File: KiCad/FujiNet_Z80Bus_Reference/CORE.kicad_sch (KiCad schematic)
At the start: 23 parts, among them IC1 74244N, IC13 7432N, IC2 7404N, IC3 7474N, IC5 7408N

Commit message: Single PCB layout experiements
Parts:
- renumbered IC1 to ESP_CONTROL_DIRECTOR1, RN1 to ESP_CONTROL_DIRECTOR_BIAS1
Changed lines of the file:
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@@
   (symbol (lib_id "FujiNet_Z80Bus_Reference-rescue:4609M-101-103LF-Z80ESP-eagle-import") (at 140.97 167.64 0) (mirror y) (unit 1)
     (in_bom yes) (on_board yes) (dnp no)
-    (property "Reference" "RN1" (at 128.27 171.45 90)
-      (effects (font (size 1.4986 1.4986)) (justify left))
+    (property "Reference" "ESP_CONTROL_DIRECTOR_BIAS1" (at 128.27 171.45 90)
+      (effects (font (size 1.4986 1.4986)))
     )
     (property "Value" "4609M-101-103LF" (at 130.81 189.23 90)
@@
       (project "FujiNet_Z80Bus_Reference"
         (path "/532c0392-800e-45cc-8170-6d32f2390e83/00000000-0000-0000-0000-000068f578e9"
-          (reference "RN1") (unit 1)
+          (reference "ESP_CONTROL_DIRECTOR_BIAS1") (unit 1)
         )
         (path "/532c0392-800e-45cc-8170-6d32f2390e83/00000000-0000-0000-0000-000068f578e9/00000000-0000-0000-0000-000068fd7452"
@@
   (symbol (lib_id "FujiNet_Z80Bus_Reference-rescue:74244N-Z80ESP-eagle-import") (at 88.9 153.67 0) (unit 1)
     (in_bom yes) (on_board yes) (dnp no)
-    (property "Reference" "IC1" (at 90.17 157.48 90)
-      (effects (font (size 1.4986 1.4986)) (justify left bottom))
+    (property "Reference" "ESP_CONTROL_DIRECTOR1" (at 90.17 157.48 90)
+      (effects (font (size 1.4986 1.4986)))
     )
     (property "Value" "74244N" (at 81.28 166.37 0)
@@
       (project "FujiNet_Z80Bus_Reference"
         (path "/532c0392-800e-45cc-8170-6d32f2390e83/00000000-0000-0000-0000-000068f578e9"
-          (reference "IC1") (unit 1)
+          (reference "ESP_CONTROL_DIRECTOR1") (unit 1)
         )
         (path "/532c0392-800e-45cc-8170-6d32f2390e83/00000000-0000-0000-0000-000068f578e9/00000000-0000-0000-0000-000068fd7452"
@@
   (symbol (lib_id "FujiNet_Z80Bus_Reference-rescue:74244N-Z80ESP-eagle-import") (at 88.9 172.72 0) (unit 2)
     (in_bom yes) (on_board yes) (dnp no)
-    (property "Reference" "IC1" (at 90.17 176.53 90)
-      (effects (font (size 1.4986 1.4986)) (justify left bottom))
+    (property "Reference" "ESP_CONTROL_DIRECTOR1" (at 90.17 176.53 90)
+      (effects (font (size 1.4986 1.4986)))
     )
     (property "Value" "74244N" (at 81.28 185.42 0)
@@
       (project "FujiNet_Z80Bus_Reference"
         (path "/532c0392-800e-45cc-8170-6d32f2390e83/00000000-0000-0000-0000-000068f578e9"
-          (reference "IC1") (unit 2)
-        )
-        (path "/532c0392-800e-45cc-8170-6d32f2390e83/00000000-0000-0000-0000-000068f578e9/00000000-0000-0000-0000-000068fd7452"
+          (reference "ESP_CONTROL_DIRECTOR1") (unit 2)
+        )
+        (path "/532c0392-800e-45cc-8170-6d32f2390e83/00000000-0000-0000-0000-000068f578e9/00000000-0000-0000-0000-000068fd7452"

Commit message: Massive fix to KiCad Labels
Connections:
- net ESP_INT: now also R?.1; no longer R?.2
- net GND: now also R?.2; no longer R?.1
- net VCC: no longer D5.2 (A), R?.1, U?.19 (+5v), U?.20 (+5V)
- net ESP_CONTROL_IORQ renamed ESP_CONTROL.IORQ
- net ESP_CONTROL_MEMRQ renamed ESP_CONTROL.MEMRQ
- net ESP_CONTROL_RD renamed ESP_CONTROL.RD
- net ESP_CONTROL_WR renamed ESP_CONTROL.WR
- net ESP_SPI.CE renamed ESP_SPI_INT.CE
- net ESP_SPI.MISO renamed ESP_SPI_INT.MISO
- net ESP_SPI.MOSI renamed ESP_SPI_INT.MOSI
- net ESP_SPI.OE renamed ESP_SPI_INT.OE
- net ESP_SPI.PL renamed ESP_SPI_INT.PL
- net ESP_SPI.SCK renamed ESP_SPI_INT.SCK
- net ESP_SPI.STC renamed ESP_SPI_INT.STC
- net LOCAL_IORQ renamed LOCAL_CONTROL.IORQ
- net LOCAL_CONTROL.IORQ: now also ESP_CONTROL_DIRECTOR_BIAS1.4; no longer ESP_CONTROL_DIRECTOR_BIAS1.5
- net LOCAL_MEMRQ renamed LOCAL_CONTROL.MEMRQ
- net LOCAL_CONTROL.MEMRQ: now also ESP_CONTROL_DIRECTOR_BIAS1.5; no longer ESP_CONTROL_DIRECTOR_BIAS1.4
- net LOCAL_RD renamed LOCAL_CONTROL.RD
- net LOCAL_WR renamed LOCAL_CONTROL.WR
- net ROM_WR_PROTECT renamed ESP_ROM_WR_PROTECT
- net Z80_BUSACK renamed Z80_CONTROL.BUSACK
- net Z80_IORQ renamed Z80_CONTROL.IORQ
- net Z80_MEMRQ renamed Z80_CONTROL.MEMRQ
- net Z80_RD renamed Z80_CONTROL.RD
- net Z80_RESET renamed Z80_CONTROL.RESET
- net Z80_WAIT renamed Z80_CONTROL.WAIT
- net Z80_WR renamed Z80_CONTROL.WR
- new net +5V: D5.2 (A), R?.1, U?.19 (+5v), U?.20 (+5V)
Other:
- sheet SPIBUS ports: added LOCAL_A[0..15], LOCAL_D[0..7], {ESP_CONTROL}, {ESP_SPI_INTERNAL}, {Z80_CONTROL}; removed ESP_CONTROL_BUSRQ, ESP_CONTROL_IORQ, ESP_CONTROL_MEMRQ, ESP_CONTROL_NMI, ESP_CONTROL_RD, ESP_CONTROL_ROMCS, ESP_CONTROL_WAIT, ESP_CONTROL_WR, ESP_PULSE, ESP_SPI.CE, ESP_SPI.MISO, ESP_SPI.MOSI, ESP_SPI.OE, ESP_SPI.PL, ESP_SPI.SCK, ESP_SPI.STC, LOCAL_ADD_[0..15], LOCAL_DATA_[0..7], Z80_BUSACK, Z80_BUSRQ, Z80_IORQ, Z80_MEMRQ, Z80_NMI, Z80_RD, Z80_ROMCS, Z80_WAIT, Z80_WR
- moved on the sheet: C1, C2, D13, D2, D3, D5, D?, ESP_CONTROL_DIRECTOR1A, ESP_CONTROL_DIRECTOR1B, ESP_CONTROL_DIRECTOR_BIAS1, EX_SPI1, IC13A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

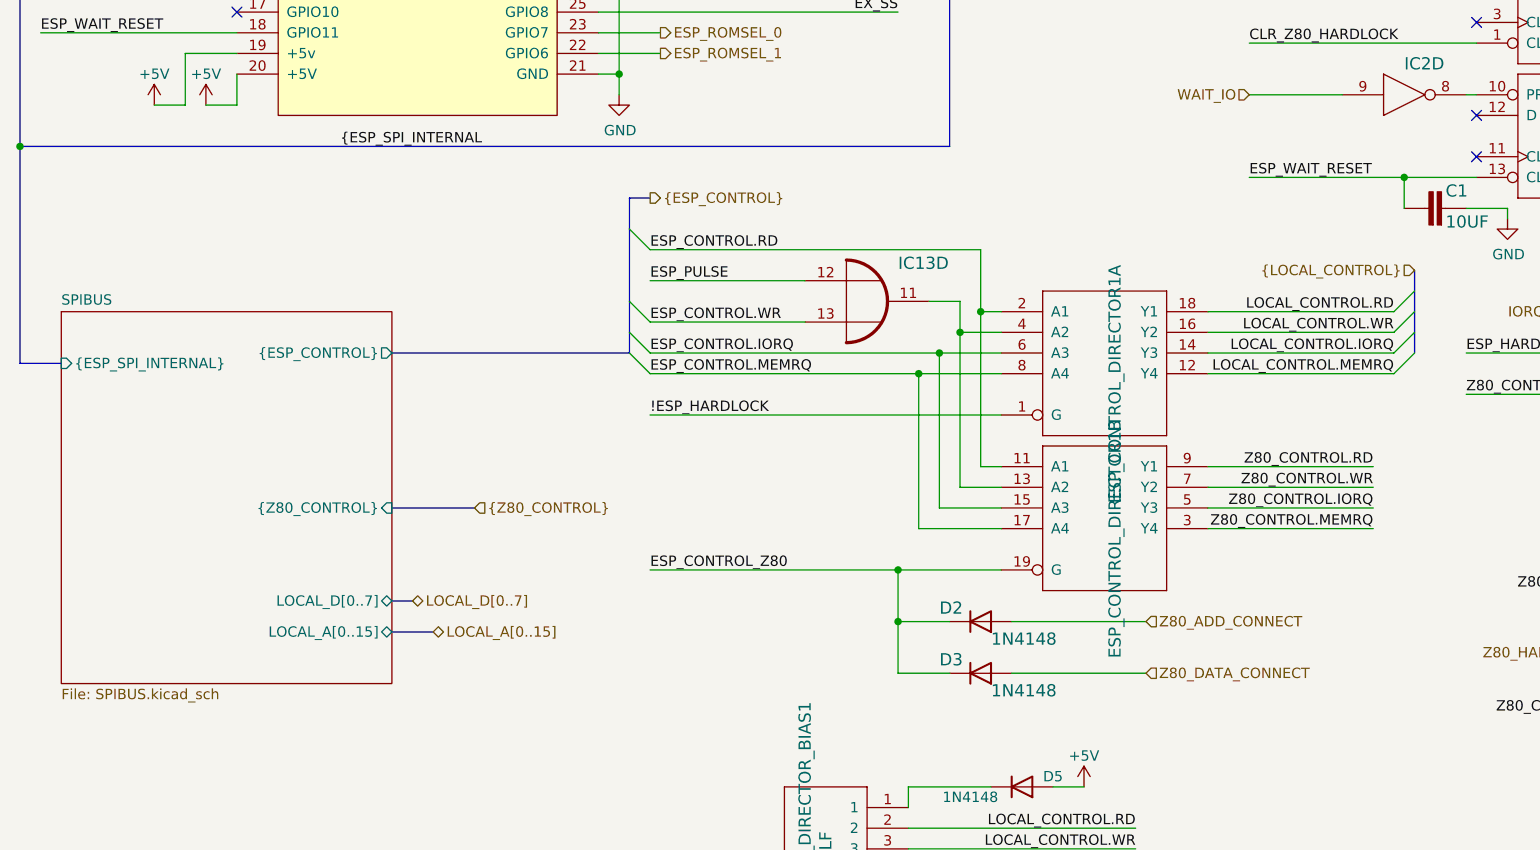
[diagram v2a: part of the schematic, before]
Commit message: KiCad Labels mostly fixed
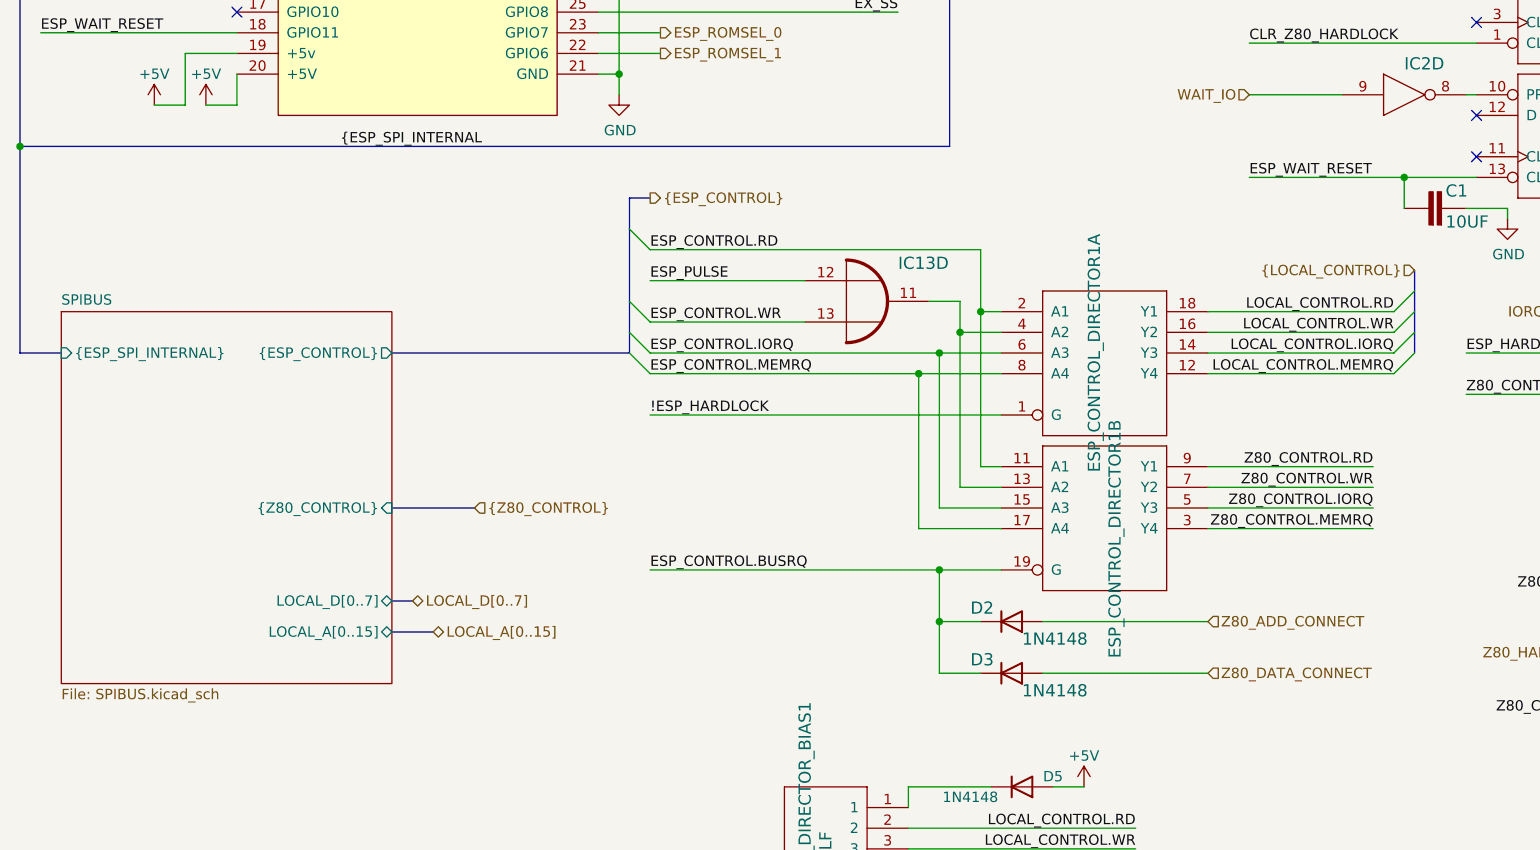
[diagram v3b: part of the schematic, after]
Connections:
- net ESP_CONTROL_Z80 renamed ESP_CONTROL.BUSRQ
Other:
- moved on the sheet: D2, D3
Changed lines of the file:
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@@
   (junction (at 19.05 86.36) (diameter 0) (color 0 0 0 0)
   )
-  (junction (at 127 144.78) (diameter 0) (color 0 0 0 0)
+  (junction (at 132.08 144.78) (diameter 0) (color 0 0 0 0)
   )
   (junction (at 189.23 90.17) (diameter 0) (color 0 0 0 0)
   )
-  (junction (at 127 138.43) (diameter 0) (color 0 0 0 0)
-  )
   (junction (at 238.76 148.59) (diameter 0) (color 0 0 0 0)
   )
@@
   )
   (junction (at 129.54 114.3) (diameter 0) (color 0 0 0 0)
+  )
+  (junction (at 132.08 138.43) (diameter 0) (color 0 0 0 0)
   )
   (no_connect (at 90.17 62.23))
@@
     (stroke (width 0) (type default))
   )
+  (wire (pts (xy 132.08 138.43) (xy 139.7 138.43))
+    (stroke (width 0) (type default))
+  )
   (bus (pts (xy 19.05 86.36) (xy 19.05 49.53))
     (stroke (width 0) (type default))
@@
     (stroke (width 0) (type default))
   )
-  (wire (pts (xy 157.48 151.13) (xy 140.97 151.13))
+  (wire (pts (xy 165.1 151.13) (xy 144.78 151.13))
     (stroke (width 0) (type default))
   )
@@
     (stroke (width 0) (type default))
   )
-  (wire (pts (xy 96.52 138.43) (xy 127 138.43))
-    (stroke (width 0) (type default))
-  )
   (wire (pts (xy 271.78 26.67) (xy 256.54 26.67))
     (stroke (width 0) (type default))
@@
     (stroke (width 0) (type default))
   )
-  (wire (pts (xy 127 151.13) (xy 133.35 151.13))
+  (wire (pts (xy 132.08 151.13) (xy 137.16 151.13))
     (stroke (width 0) (type default))
   )
@@
     (stroke (width 0) (type default))
   )
-  (wire (pts (xy 127 138.43) (xy 127 144.78))
+  (wire (pts (xy 132.08 138.43) (xy 132.08 144.78))
     (stroke (width 0) (type default))
   )
@@
     (stroke (width 0) (type default))
   )
-  (wire (pts (xy 157.48 144.78) (xy 140.97 144.78))
+  (wire (pts (xy 165.1 144.78) (xy 144.78 144.78))
     (stroke (width 0) (type default))
   )
@@
     (stroke (width 0) (type default))
   )
-  (wire (pts (xy 127 144.78) (xy 133.35 144.78))
+  (wire (pts (xy 132.08 144.78) (xy 137.16 144.78))
     (stroke (width 0) (type default))
   )
@@
     (stroke (width 0) (type default))
   )
-  (bus (pts (xy 19.05 113.03) (xy 24.13 113.03))
+  (bus (pts (xy 19.05 111.76) (xy 24.13 111.76))
     (stroke (width 0) (type default))
   )
@@
     (stroke (width 0) (type default))
   )
-  (bus (pts (xy 19.05 86.36) (xy 19.05 113.03))
+  (bus (pts (xy 19.05 86.36) (xy 19.05 111.76))
     (stroke (width 0) (type default))
   )
@@
     (stroke (width 0) (type default))
   )
-  (wire (pts (xy 127 138.43) (xy 139.7 138.43))
-    (stroke (width 0) (type default))
-  )
   (wire (pts (xy 137.16 99.06) (xy 137.16 106.68))
     (stroke (width 0) (type default))
@@
     (stroke (width 0) (type default))
   )
+  (wire (pts (xy 96.52 138.43) (xy 132.08 138.43))
+    (stroke (width 0) (type default))
+  )
   (wire (pts (xy 189.23 93.98) (xy 189.23 90.17))
     (stroke (width 0) (type default))
@@
     (stroke (width 0) (type default))
   )
-  (wire (pts (xy 127 151.13) (xy 127 144.78))
+  (wire (pts (xy 132.08 151.13) (xy 132.08 144.78))
     (stroke (width 0) (type default))
   )
@@
     (effects (font (size 1.27 1.27)) (justify right bottom))
   )
-  (label "ESP_CONTROL_Z80" (at 96.52 138.43 0) (fields_autoplaced)
-    (effects (font (size 1.27 1.27)) (justify left bottom))
-  )
   (label "ESP_HARDLOCK" (at 170.18 22.86 0) (fields_autoplaced)
     (effects (font (size 1.27 1.27)) (justify left bottom))
   )
+  (label "ESP_CONTROL.BUSRQ" (at 96.52 138.43 0) (fields_autoplaced)
+    (effects (font (size 1.27 1.27)) (justify left bottom))
+  )
   (label "GND" (at 256.54 34.29 0) (fields_autoplaced)
     (effects (font (size 1.27 1.27)) (justify left bottom))
@@
     (effects (font (size 1.27 1.27)) (justify right bottom))
   )
-  (hierarchical_label "Z80_DATA_CONNECT" (shape input) (at 157.48 151.13 0) (fields_autoplaced)
+  (hierarchical_label "Z80_DATA_CONNECT" (shape input) (at 165.1 151.13 0) (fields_autoplaced)
     (effects (font (size 1.27 1.27)) (justify left))
   )
@@
     (effects (font (size 1.27 1.27)) (justify left))
   )
-  (hierarchical_label "Z80_ADD_CONNECT" (shape input) (at 157.48 144.78 0) (fields_autoplaced)
+  (hierarchical_label "Z80_ADD_CONNECT" (shape input) (at 165.1 144.78 0) (fields_autoplaced)
     (effects (font (size 1.27 1.27)) (justify left))
   )
@@
     )
   )
-  (symbol (lib_id "Device:D") (at 137.16 151.13 0) (mirror x) (unit 1)
-    (in_bom yes) (on_board yes) (dnp no)
-    (property "Reference" "D3" (at 132.08 148.59 0)
-      (effects (font (size 1.4986 1.4986)) (justify left bottom))
-    )
-    (property "Value" "1N4148" (at 138.43 152.4 0)
-      (effects (font (size 1.4986 1.4986)) (justify left bottom))
-    )
-    (property "Footprint" "Diode_THT:D_T-1_P5.08mm_Horizontal" (at 137.16 151.13 0)
-      (effects (font (size 1.27 1.27)) hide)
-    )
-    (property "Datasheet" "" (at 137.16 151.13 0)
+  (symbol (lib_id "Device:D") (at 140.97 151.13 0) (mirror x) (unit 1)
+    (in_bom yes) (on_board yes) (dnp no)
+    (property "Reference" "D3" (at 135.89 148.59 0)
+      (effects (font (size 1.4986 1.4986)) (justify left bottom))
+    )
+    (property "Value" "1N4148" (at 142.24 152.4 0)
+      (effects (font (size 1.4986 1.4986)) (justify left bottom))
+    )
+    (property "Footprint" "Diode_THT:D_T-1_P5.08mm_Horizontal" (at 140.97 151.13 0)
+      (effects (font (size 1.27 1.27)) hide)
+    )
+    (property "Datasheet" "" (at 140.97 151.13 0)
       (effects (font (size 1.27 1.27)) hide)
     )
@@
     )
   )
-  (symbol (lib_id "Device:D") (at 137.16 144.78 0) (mirror x) (unit 1)
-    (in_bom yes) (on_board yes) (dnp no)
-    (property "Reference" "D2" (at 132.08 142.24 0)
-      (effects (font (size 1.4986 1.4986)) (justify left bottom))
-    )
-    (property "Value" "1N4148" (at 138.43 146.05 0)
-      (effects (font (size 1.4986 1.4986)) (justify left bottom))
-    )
-    (property "Footprint" "Diode_THT:D_T-1_P5.08mm_Horizontal" (at 137.16 144.78 0)
-      (effects (font (size 1.27 1.27)) hide)
-    )
-    (property "Datasheet" "" (at 137.16 144.78 0)
+  (symbol (lib_id "Device:D") (at 140.97 144.78 0) (mirror x) (unit 1)
+    (in_bom yes) (on_board yes) (dnp no)
+    (property "Reference" "D2" (at 135.89 142.24 0)
+      (effects (font (size 1.4986 1.4986)) (justify left bottom))
+    )
+    (property "Value" "1N4148" (at 142.24 146.05 0)
+      (effects (font (size 1.4986 1.4986)) (justify left bottom))
+    )
+    (property "Footprint" "Diode_THT:D_T-1_P5.08mm_Horizontal" (at 140.97 144.78 0)
+      (effects (font (size 1.27 1.27)) hide)
+    )
+    (property "Datasheet" "" (at 140.97 144.78 0)
       (effects (font (size 1.27 1.27)) hide)
     )
@@
   (symbol (lib_id "FujiNet_Z80Bus_Reference-rescue:74244N-Z80ESP-eagle-import") (at 152.4 111.76 0) (unit 1)
     (in_bom yes) (on_board yes) (dnp no)
-    (property "Reference" "ESP_CONTROL_DIRECTOR1" (at 153.67 115.57 90)
+    (property "Reference" "ESP_CONTROL_DIRECTOR1" (at 151.13 111.76 90)
       (effects (font (size 1.4986 1.4986)))
     )
@@
     (pin "7")
     (pin "9")
-    (pin "10")
-    (pin "20")
     (instances
       (project "FujiNet_Z80Bus_Reference"
@@
     )
   )
-  (symbol (lib_id "FujiNet_Z80Bus_Reference-rescue:74244N-Z80ESP-eagle-import") (at 152.4 130.81 0) (unit 2)
+  (symbol (lib_name "74244N-Z80ESP-eagle-import_1") (lib_id "FujiNet_Z80Bus_Reference-rescue:74244N-Z80ESP-eagle-import") (at 152.4 130.81 0) (unit 2)
     (in_bom yes) (on_board yes) (dnp no)
     (property "Reference" "ESP_CONTROL_DIRECTOR1" (at 153.67 134.62 90)
@@
     (pin "7")
     (pin "9")
-    (pin "10")
-    (pin "20")
     (instances
       (project "FujiNet_Z80Bus_Reference"
@@
       (effects (font (size 1.27 1.27)) (justify right))
     )
-    (pin "{ESP_SPI_INTERNAL}" input (at 24.13 113.03 180)
+    (pin "{ESP_SPI_INTERNAL}" input (at 24.13 111.76 180)
       (effects (font (size 1.27 1.27)) (justify left))
     )
